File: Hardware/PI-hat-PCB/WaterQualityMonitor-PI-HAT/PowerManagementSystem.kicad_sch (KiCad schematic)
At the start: 0 parts

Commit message: started design on PMS added components and values
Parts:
- added C? (x2): 470uF, symbol Device:C_Polarized
- added C? (x2): 0.1uF, symbol Device:C
- added D?: TSSA3U45, DIOM5126X250N, symbol SamacSys_Parts:TSSA3U45
- added IC? (x3): TS2596CM550_RNG, TS2596CM550RNG, symbol SamacSys_Parts:TS2596CM550_RNG
- added J?: Jack-DC 24V in, symbol Connector:Jack-DC
- added L?: 33uH, symbol Device:L
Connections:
- new net: IC?.3 (GROUND_1), IC?.6 (GROUND_2) (x3)

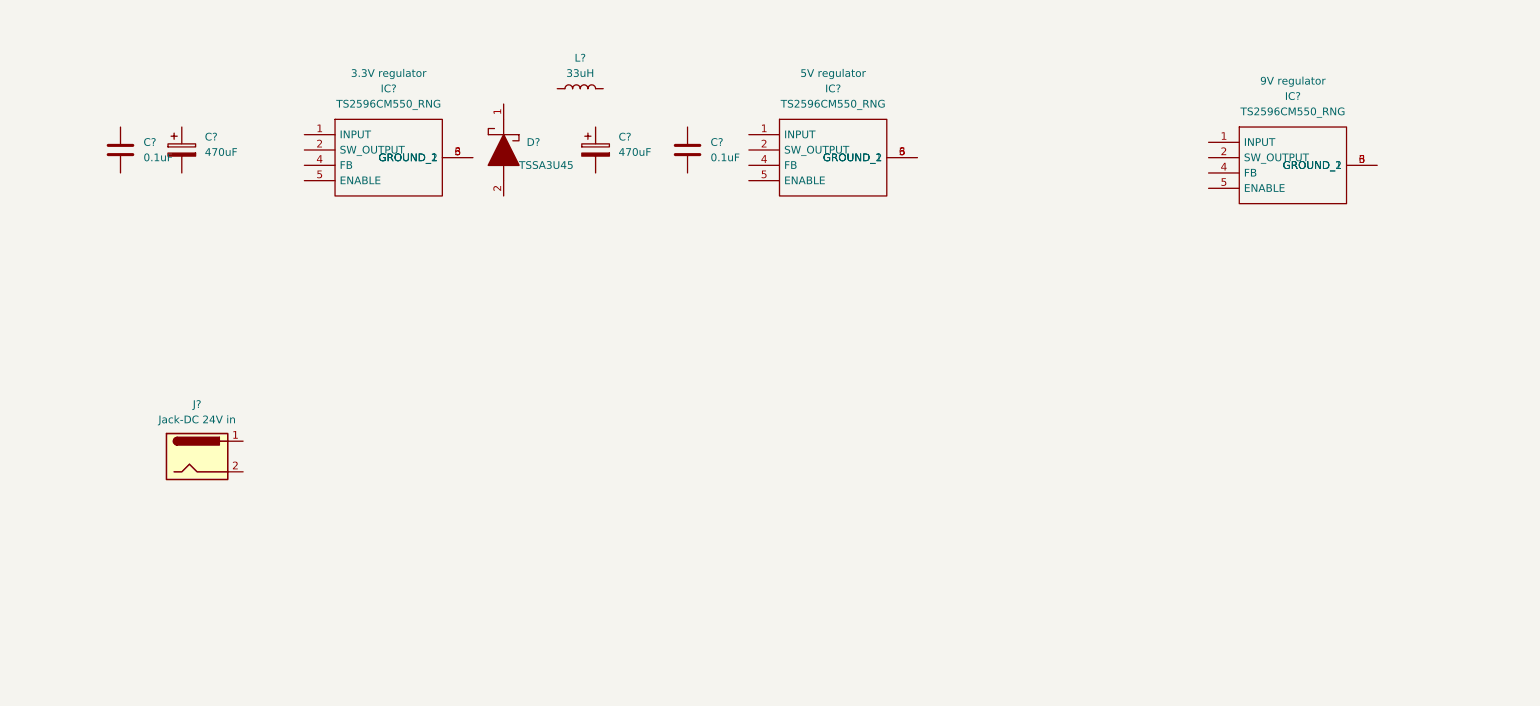
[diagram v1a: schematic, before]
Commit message: finished creating power regulator circuits
for 9V,5V and 3.3V
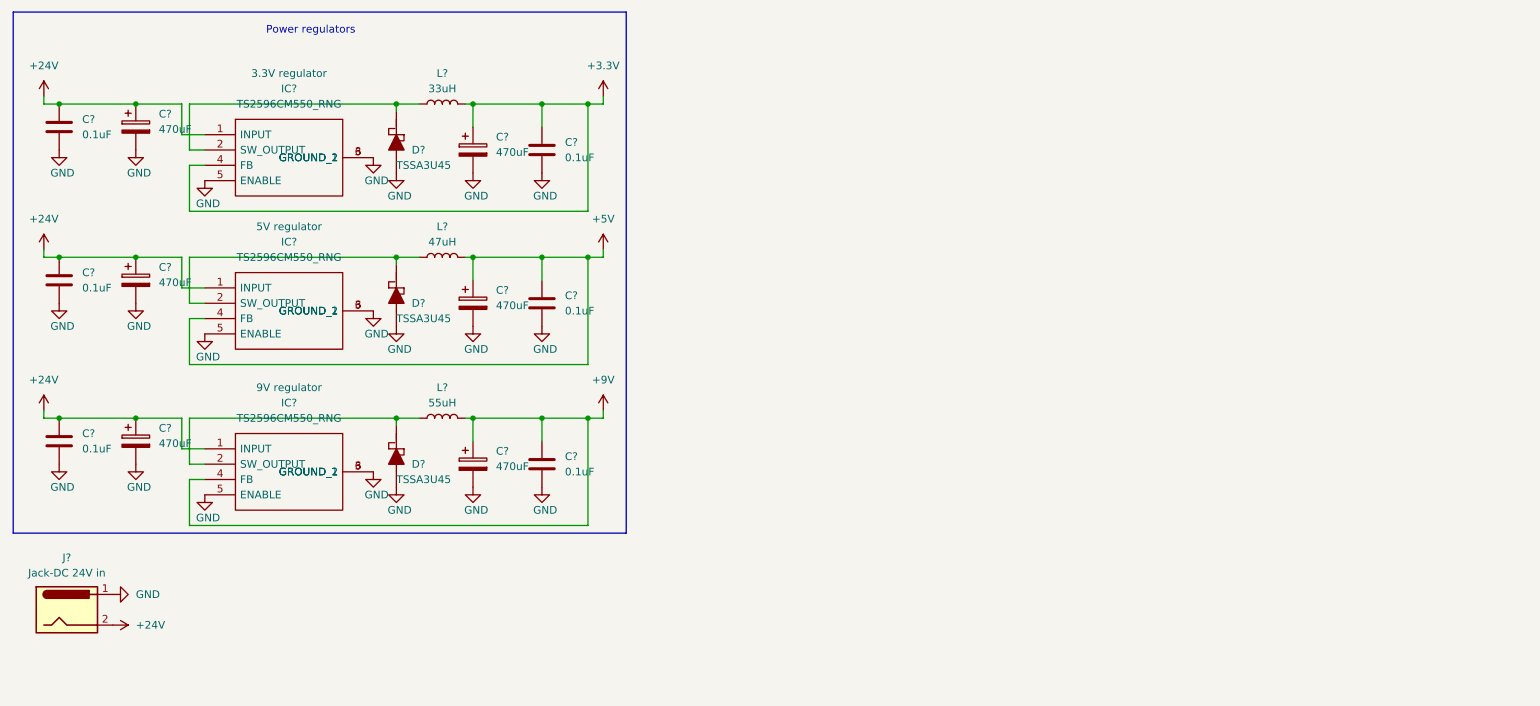
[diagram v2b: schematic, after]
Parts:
- removed IC? (x2): TS2596CM550_RNG, TS2596CM550RNG, symbol SamacSys_Parts:TS2596CM550_RNG
- added C? (x4): 0.1uF, symbol Device:C
- added C? (x4): 470uF, symbol Device:C_Polarized
- added D? (x2): TSSA3U45, DIOM5126X250N, symbol SamacSys_Parts:TSSA3U45
- added IC? (x2): TS2596CM550_RNG, TS2596CM550RNG, symbol SamacSys_Parts:TS2596CM550_RNG
- added L?: 47uH, symbol Device:L
- added L?: 55uH, symbol Device:L
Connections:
- net at L?.1: now also D?., IC?.2 (SW_OUTPUT)
- net +3.3V: now reaches L?.2
- net +3.3V: now also C?.1, C?.1, IC?.4 (FB)
- net +24V: now reaches IC?.1 (INPUT)
- net +24V: now also C?.1, C?.1, J?.2, C?.1, C?.1, C?.1, C?.1, IC?.1 (INPUT), IC?.1 (INPUT)
- net GND: now reaches IC?.3 (GROUND_1), IC?.6 (GROUND_2)
- net GND: now also C?.2, C?.2, C?.2, C?.2, D?., IC?.5 (ENABLE), J?.1, C?.2, C?.2, C?.2, C?.2, C?.2, C?.2, C?.2, C?.2, D?., D?., IC?.3 (GROUND_1), IC?.3 (GROUND_1), IC?.5 (ENABLE), IC?.5 (ENABLE), IC?.6 (GROUND_2), IC?.6 (GROUND_2)
- new net: D?., IC?.2 (SW_OUTPUT), L?.1 (x2)
- new net +5V: C?.1, C?.1, IC?.4 (FB), L?.2
- new net +9V: C?.1, C?.1, IC?.4 (FB), L?.2
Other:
- note added: "Power regulators"
- moved on the sheet: C?, IC?, J?, L?

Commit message: changed to 2*5V power supply
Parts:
- IC?: Purpose 5V regulator -> 5V regulator 1
- IC?: Purpose 9V regulator -> 5V regulator 2
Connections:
- net +9V is gone; now on net +5V: C?.1, C?.1, IC?.4 (FB), L?.2
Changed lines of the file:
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@@
-    (pin "1")
-  )
-  (symbol (lib_id "power:+9V") (at 110.49 78.74 0) (unit 1)
-    (in_bom yes) (on_board yes) (fields_autoplaced)
-    (property "Reference" "#PWR?" (id 0) (at 110.49 82.55 0)
-      (effects (font (size 1.27 1.27)) hide)
-    )
-    (property "Value" "+9V" (id 1) (at 110.49 73.66 0))
-    (property "Footprint" "" (id 2) (at 110.49 78.74 0)
-      (effects (font (size 1.27 1.27)) hide)
-    )
-    (property "Datasheet" "" (id 3) (at 110.49 78.74 0)
-      (effects (font (size 1.27 1.27)) hide)
-    )
     (pin "1")
   )
@@
     )
     (property "Datasheet" "" (id 3) (at 72.39 88.9 0)
+      (effects (font (size 1.27 1.27)) hide)
+    )
+    (pin "1")
+  )
+  (symbol (lib_id "power:+5V") (at 110.49 78.74 0) (unit 1)
+    (in_bom yes) (on_board yes) (fields_autoplaced)
+    (property "Reference" "#PWR?" (id 0) (at 110.49 82.55 0)
+      (effects (font (size 1.27 1.27)) hide)
+    )
+    (property "Value" "+5V" (id 1) (at 110.49 73.66 0))
+    (property "Footprint" "" (id 2) (at 110.49 78.74 0)
+      (effects (font (size 1.27 1.27)) hide)
+    )
+    (property "Datasheet" "" (id 3) (at 110.49 78.74 0)
       (effects (font (size 1.27 1.27)) hide)
     )
@@
       (effects (font (size 1.27 1.27)) (justify left) hide)
     )
-    (property "Purpose" "5V regulator" (id 10) (at 58.42 48.26 0))
+    (property "Purpose" "5V regulator 1" (id 10) (at 58.42 48.26 0))
     (pin "1")
     (pin "2")
@@
       (effects (font (size 1.27 1.27)) (justify left) hide)
     )
-    (property "Purpose" "9V regulator" (id 10) (at 58.42 74.93 0))
-    (pin "1")
-    (pin "2")
+    (property "Purpose" "5V regulator 2" (id 10) (at 58.42 74.93 0))
+    (pin "1")
+    (pin "2")

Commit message: removed old regulator circuits
a better chip (tested) has been found rt7272a
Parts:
- L?: value 55uH -> 47uH
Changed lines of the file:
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@@
     (in_bom yes) (on_board yes)
     (property "Reference" "L?" (id 0) (at 83.82 74.93 90))
-    (property "Value" "55uH" (id 1) (at 83.82 77.47 90))
+    (property "Value" "47uH" (id 1) (at 83.82 77.47 90))
     (property "Footprint" "" (id 2) (at 83.82 80.01 0)
       (effects (font (size 1.27 1.27)) hide)

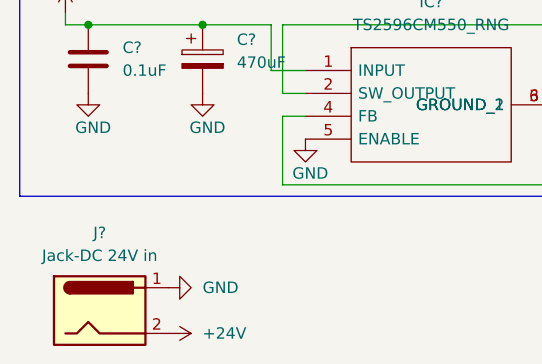
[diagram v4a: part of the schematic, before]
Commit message: Finished Motor drivers and started PMS again
Now I actually removed the power management system
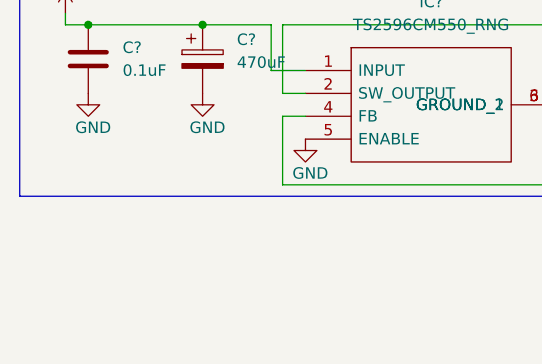
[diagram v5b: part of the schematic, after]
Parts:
- removed J?: Jack-DC 24V in, symbol Connector:Jack-DC
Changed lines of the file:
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@@
     (pin "2")
-  )
-  (symbol (lib_id "power:+24V") (at 29.21 114.3 270) (unit 1)
-    (in_bom yes) (on_board yes) (fields_autoplaced)
-    (property "Reference" "#PWR?" (id 0) (at 25.4 114.3 0)
-      (effects (font (size 1.27 1.27)) hide)
-    )
-    (property "Value" "+24V" (id 1) (at 33.02 114.2999 90)
-      (effects (font (size 1.27 1.27)) (justify left))
-    )
-    (property "Footprint" "" (id 2) (at 29.21 114.3 0)
-      (effects (font (size 1.27 1.27)) hide)
-    )
-    (property "Datasheet" "" (id 3) (at 29.21 114.3 0)
-      (effects (font (size 1.27 1.27)) hide)
-    )
-    (pin "1")
   )
   (symbol (lib_id "Device:C") (at 100.33 60.96 0) (unit 1)
@@
     (pin "1")
   )
-  (symbol (lib_id "Connector:Jack-DC") (at 21.59 111.76 0) (unit 1)
-    (in_bom yes) (on_board yes) (fields_autoplaced)
-    (property "Reference" "J?" (id 0) (at 21.59 103.124 0))
-    (property "Value" "Jack-DC 24V in" (id 1) (at 21.59 105.664 0))
-    (property "Footprint" "" (id 2) (at 22.86 112.776 0)
-      (effects (font (size 1.27 1.27)) hide)
-    )
-    (property "Datasheet" "~" (id 3) (at 22.86 112.776 0)
-      (effects (font (size 1.27 1.27)) hide)
-    )
-    (pin "1")
-    (pin "2")
-  )
   (symbol (lib_id "Device:L") (at 83.82 53.34 90) (unit 1)
     (in_bom yes) (on_board yes)
@@
       (effects (font (size 1.27 1.27)) hide)
     )
-    (pin "1")
-  )
-  (symbol (lib_id "power:GND") (at 29.21 109.22 90) (unit 1)
-    (in_bom yes) (on_board yes) (fields_autoplaced)
-    (property "Reference" "#PWR?" (id 0) (at 35.56 109.22 0)
-      (effects (font (size 1.27 1.27)) hide)
-    )
-    (property "Value" "GND" (id 1) (at 33.02 109.2199 90)
-      (effects (font (size 1.27 1.27)) (justify right))
-    )
-    (property "Footprint" "" (id 2) (at 29.21 109.22 0)
-      (effects (font (size 1.27 1.27)) hide)
-    )
-    (property "Datasheet" "" (id 3) (at 29.21 109.22 0)
-      (effects (font (size 1.27 1.27)) hide)
-    )

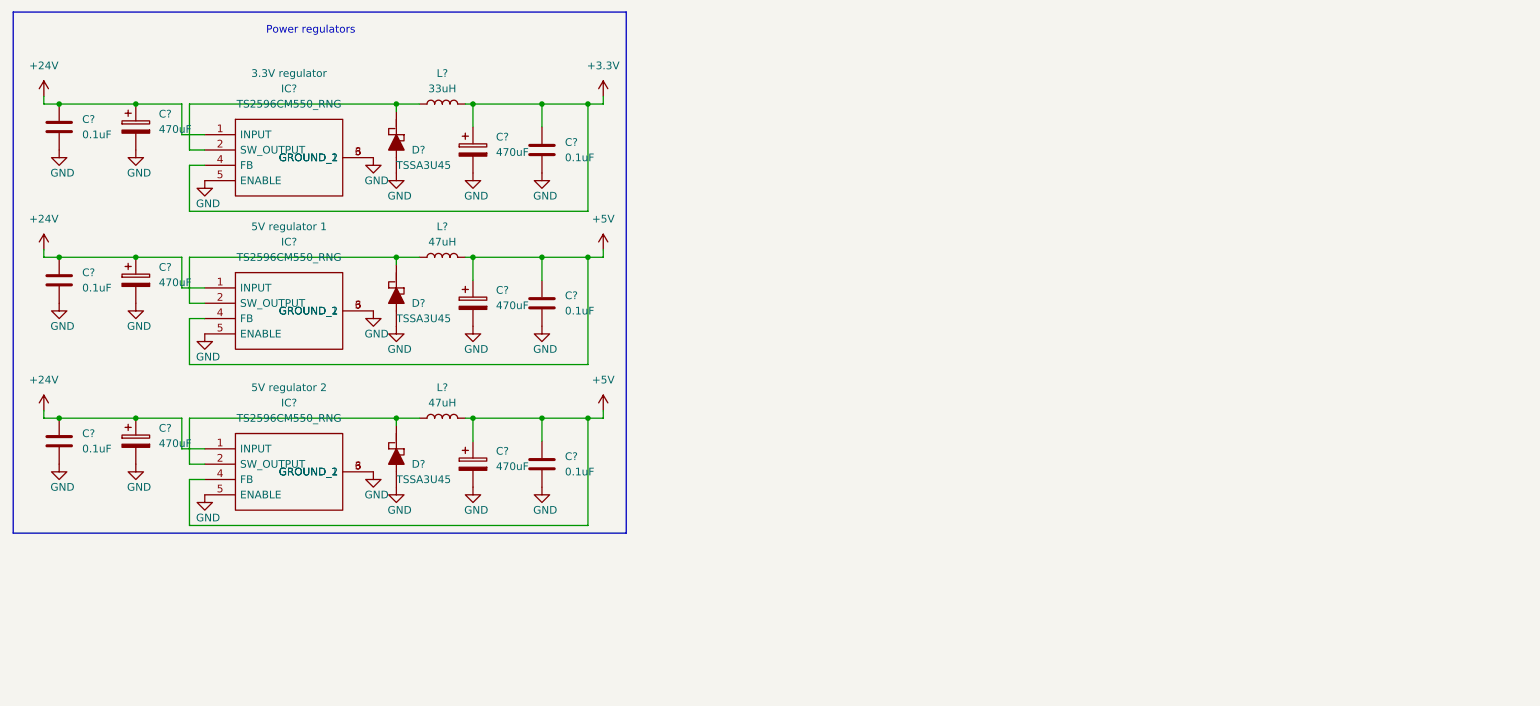
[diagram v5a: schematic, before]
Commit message: placed components
First L should be checked, possibly not the right component
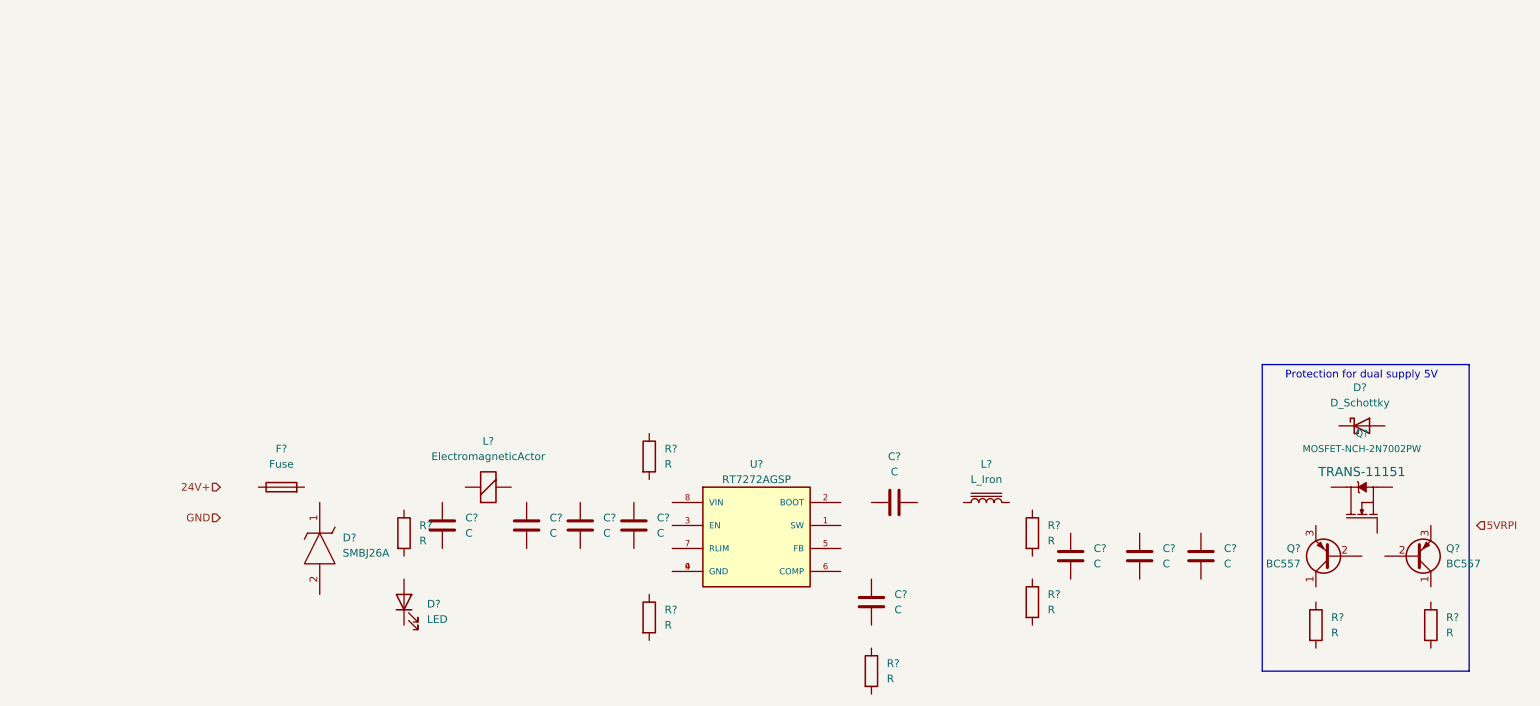
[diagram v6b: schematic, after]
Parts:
- removed C? (x6): 0.1uF, symbol Device:C
- removed C? (x6): 470uF, symbol Device:C_Polarized
- removed D? (x3): TSSA3U45, DIOM5126X250N, symbol SamacSys_Parts:TSSA3U45
- removed IC? (x3): TS2596CM550_RNG, TS2596CM550RNG, symbol SamacSys_Parts:TS2596CM550_RNG
- removed L?: 33uH, symbol Device:L
- removed L? (x2): 47uH, symbol Device:L
- added C? (x9): C, symbol Device:C
- added D?: D_Schottky, symbol Device:D_Schottky
- added D?: SMBJ26A, DIOM5436X244N, symbol SamacSys_Parts:SMBJ26A
- added D?: LED, symbol Device:LED
- added F?: Fuse, symbol Device:Fuse
- added L?: ElectromagneticActor, symbol Device:ElectromagneticActor
- added L?: L_Iron, symbol Device:L_Iron
- added Q? (x2): BC557, Package_TO_SOT_THT:TO-92_Inline, symbol Transistor_BJT:BC557
- added Q?: MOSFET-NCH-2N7002PW, SOT323, symbol SparkFun-DiscreteSemi:MOSFET-NCH-2N7002PW
- added R? (x8): R, symbol Device:R
- added U?: RT7272AGSP, SOIC127P599X175-9N, symbol RT7272AGSP:RT7272AGSP
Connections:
- new net: U?.4 (GND), U?.9 (GND)
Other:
- note added: "Protection for dual supply 5V"
- note removed: "Power regulators"
